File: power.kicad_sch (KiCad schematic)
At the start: 36 parts, among them SW2 SW_DPST

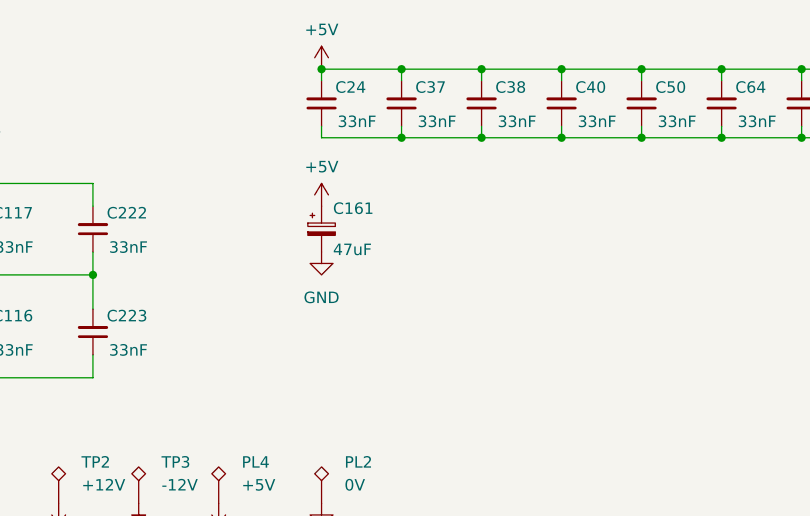
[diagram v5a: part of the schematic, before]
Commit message: wire in LA bus
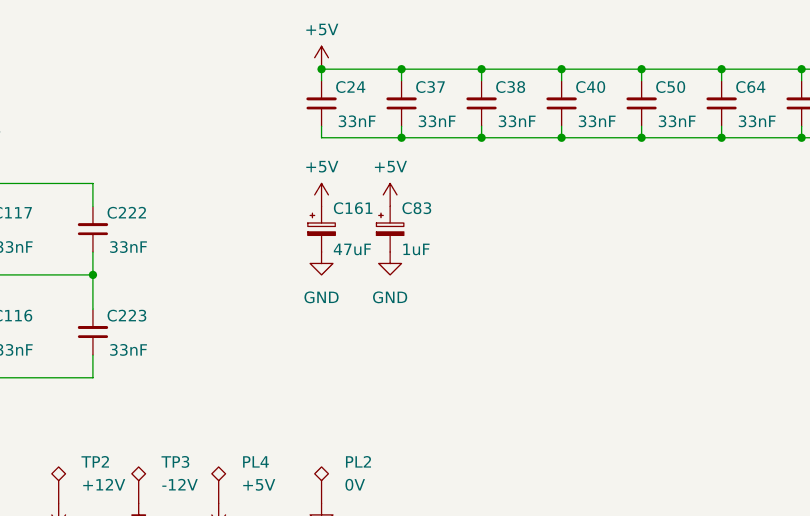
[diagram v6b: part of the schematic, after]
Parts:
- added C83: 1uF, Capacitor_THT:CP_Radial_Tantal_D8.0mm_P5.00mm, symbol Device:C_Polarized_Small
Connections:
- net +5V: now also C83.1
- net GND: now also C83.2
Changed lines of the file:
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@@
 	)
 	(symbol
+		(lib_id "power:+5V")
+		(at 140.97 36.83 0)
+		(unit 1)
+		(exclude_from_sim no)
+		(in_bom yes)
+		(on_board yes)
+		(dnp no)
+		(fields_autoplaced yes)
+		(property "Reference" "#PWR0285"
+			(at 140.97 40.64 0)
+			(effects
+				(font
+					(size 1.27 1.27)
+				)
+				(hide yes)
+			)
+		)
+		(property "Value" "+5V"
+			(at 140.97 32.4587 0)
+			(effects
+				(font
+					(size 1.27 1.27)
+				)
+			)
+		)
+		(property "Footprint" ""
+			(at 140.97 36.83 0)
+			(effects
+				(font
+					(size 1.27 1.27)
+				)
+				(hide yes)
+			)
+		)
+		(property "Datasheet" ""
+			(at 140.97 36.83 0)
+			(effects
+				(font
+					(size 1.27 1.27)
+				)
+				(hide yes)
+			)
+		)
+		(property "Description" "Power symbol creates a global label with name \"+5V\""
+			(at 140.97 36.83 0)
+			(effects
+				(font
+					(size 1.27 1.27)
+				)
+				(hide yes)
+			)
+		)
+		(pin "1"
+		)
+		(instances
+			(project "Acorn-A3010"
+				(path "/999882f3-94f8-4a89-9093-27a47d0cb289/5e8722fb-7afe-44d4-8a36-2936df1b76c5"
+					(reference "#PWR0285")
+					(unit 1)
+				)
+			)
+		)
+	)
+	(symbol
 		(lib_id "Device:C_Polarized_Small")
 		(at 133.35 39.37 0)
@@
 	)
 	(symbol
+		(lib_id "Device:C_Polarized_Small")
+		(at 140.97 39.37 0)
+		(unit 1)
+		(exclude_from_sim no)
+		(in_bom yes)
+		(on_board yes)
+		(dnp no)
+		(property "Reference" "C83"
+			(at 142.24 37.084 0)
+			(effects
+				(font
+					(size 1.27 1.27)
+				)
+				(justify left)
+			)
+		)
+		(property "Value" "1uF"
+			(at 142.24 41.656 0)
+			(effects
+				(font
+					(size 1.27 1.27)
+				)
+				(justify left)
+			)
+		)
+		(property "Footprint" "Capacitor_THT:CP_Radial_Tantal_D8.0mm_P5.00mm"
+			(at 140.97 39.37 0)
+			(effects
+				(font
+					(size 1.27 1.27)
+				)
+				(hide yes)
+			)
+		)
+		(property "Datasheet" "~"
+			(at 140.97 39.37 0)
+			(effects
+				(font
+					(size 1.27 1.27)
+				)
+				(hide yes)
+			)
+		)
+		(property "Description" "Polarized capacitor, small symbol"
+			(at 140.97 39.37 0)
+			(effects
+				(font
+					(size 1.27 1.27)
+				)
+				(hide yes)
+			)
+		)
+		(pin "2"
+		)
+		(pin "1"
+		)
+		(instances
+			(project "Acorn-A3010"
+				(path "/999882f3-94f8-4a89-9093-27a47d0cb289/5e8722fb-7afe-44d4-8a36-2936df1b76c5"
+					(reference "C83")
+					(unit 1)
+				)
+			)
+		)
+	)
+	(symbol
 		(lib_id "power:GND")
 		(at 88.9 77.47 90)
@@
 					(unit 1)
 				)
+			)
+		)
+	)
+	(symbol
+		(lib_id "power:GND")
+		(at 140.97 41.91 0)
+		(unit 1)
+		(exclude_from_sim no)
+		(in_bom yes)
+		(on_board yes)
+		(dnp no)
+		(fields_autoplaced yes)
+		(property "Reference" "#PWR0286"
+			(at 140.97 48.26 0)
+			(effects
+				(font
+					(size 1.27 1.27)
+				)
+				(hide yes)
+			)
+		)
+		(property "Value" "GND"
+			(at 140.97 46.99 0)
+			(effects
+				(font
+					(size 1.27 1.27)
+				)
+			)
+		)
+		(property "Footprint" ""
+			(at 140.97 41.91 0)
+			(effects
+				(font
+					(size 1.27 1.27)
+				)
+				(hide yes)
+			)
+		)
+		(property "Datasheet" ""
+			(at 140.97 41.91 0)
+			(effects
+				(font
+					(size 1.27 1.27)
+				)
+				(hide yes)
+			)
+		)
+		(property "Description" "Power symbol creates a global label with name \"GND\" , ground"
+			(at 140.97 41.91 0)
+			(effects
+				(font
+					(size 1.27 1.27)
+				)
+				(hide yes)
+			)
+		)
+		(pin "1"
+		)
+		(instances
+			(project "Acorn-A3010"
+				(path "/999882f3-94f8-4a89-9093-27a47d0cb289/5e8722fb-7afe-44d4-8a36-2936df1b76c5"
+					(reference "#PWR0286")
+					(unit 1)
+				)

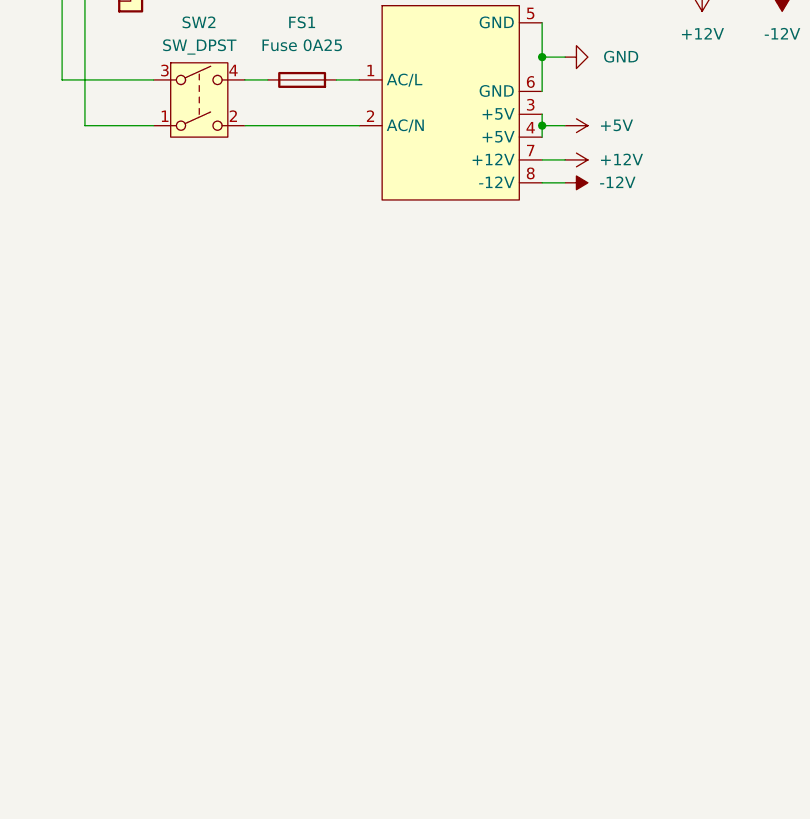
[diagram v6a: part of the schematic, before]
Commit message: video and keyboard routing
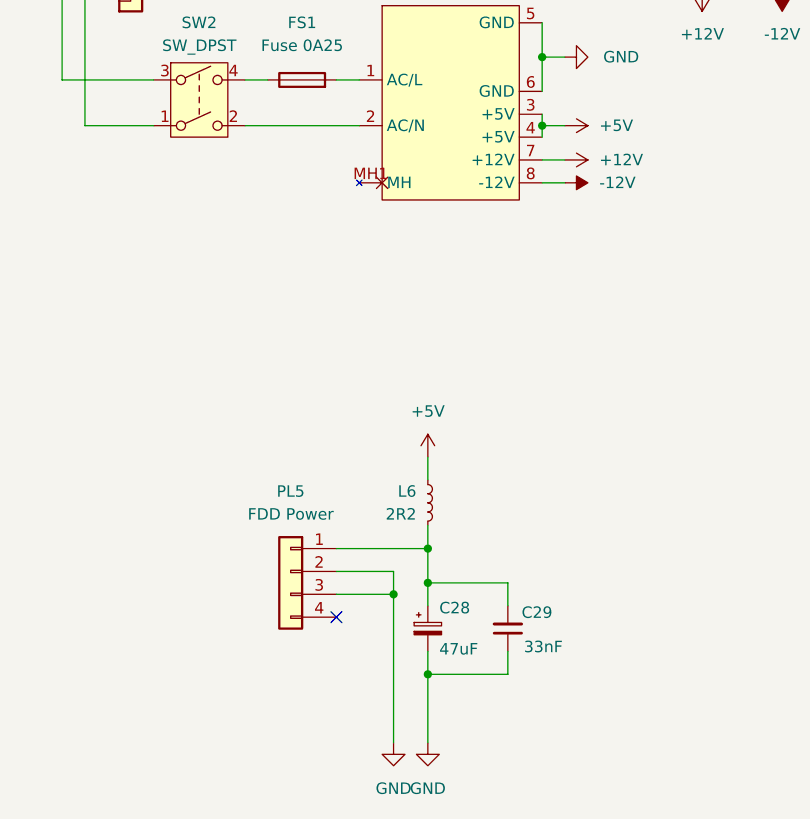
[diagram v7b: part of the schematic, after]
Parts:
- added C28: 47uF, Capacitor_THT:CP_Radial_D8.0mm_P5.00mm, symbol Device:C_Polarized_Small
- added C29: 33nF, Capacitor_SMD:C_0805_2012Metric, symbol Device:C_Small
- added L6: 2R2, Acorn:L_Acorn_8x3mm, symbol Device:L_Small
- added PL5: FDD Power, Connector_Molex:Molex_KK-254_AE-6410-04A_1x04_P2.54mm_Vertical, symbol Connector_Generic:Conn_01x04
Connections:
- net +5V: now also L6.1
- net GND: now also C28.2, C29.1, PL5.2 (Pin_2), PL5.3 (Pin_3)
- new net: C28.1, C29.2, L6.2, PL5.1 (Pin_1)
- no-connect marks 0 -> 1

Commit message: keyboard and joystick routing
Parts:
- added C103: 33nF, Capacitor_SMD:C_0805_2012Metric, symbol Device:C_Small
- added C39: 220uF, Capacitor_THT:CP_Radial_Tantal_D8.0mm_P5.00mm, symbol Device:C_Polarized_Small
- C83: value 1uF -> 10uF
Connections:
- net +5V: now also C103.2, C39.1
- net GND: now also C103.1, C39.2
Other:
- moved on the sheet: C138, C151, C227
